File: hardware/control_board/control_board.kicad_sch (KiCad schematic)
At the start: 31 parts, among them J1 SWD, J2 Panel, J3 I2C, J4 SPI, SW1 Reset, U1 STM32F103C8T6, Y1 8MHz

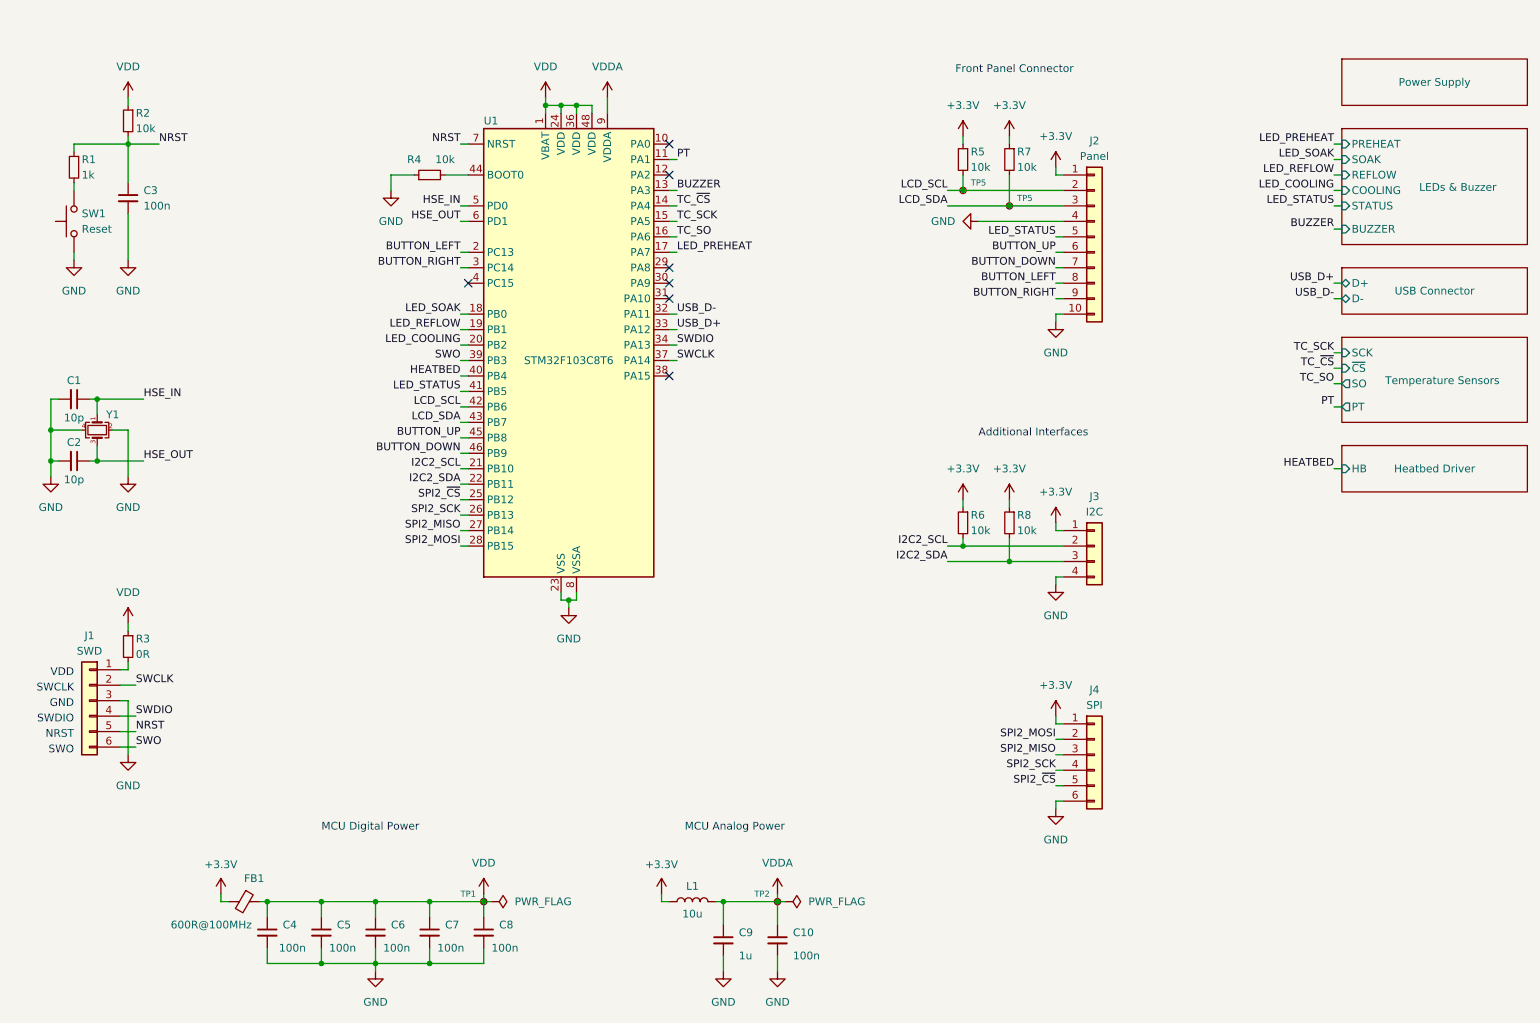
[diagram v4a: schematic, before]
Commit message: Place components on the control board PCB
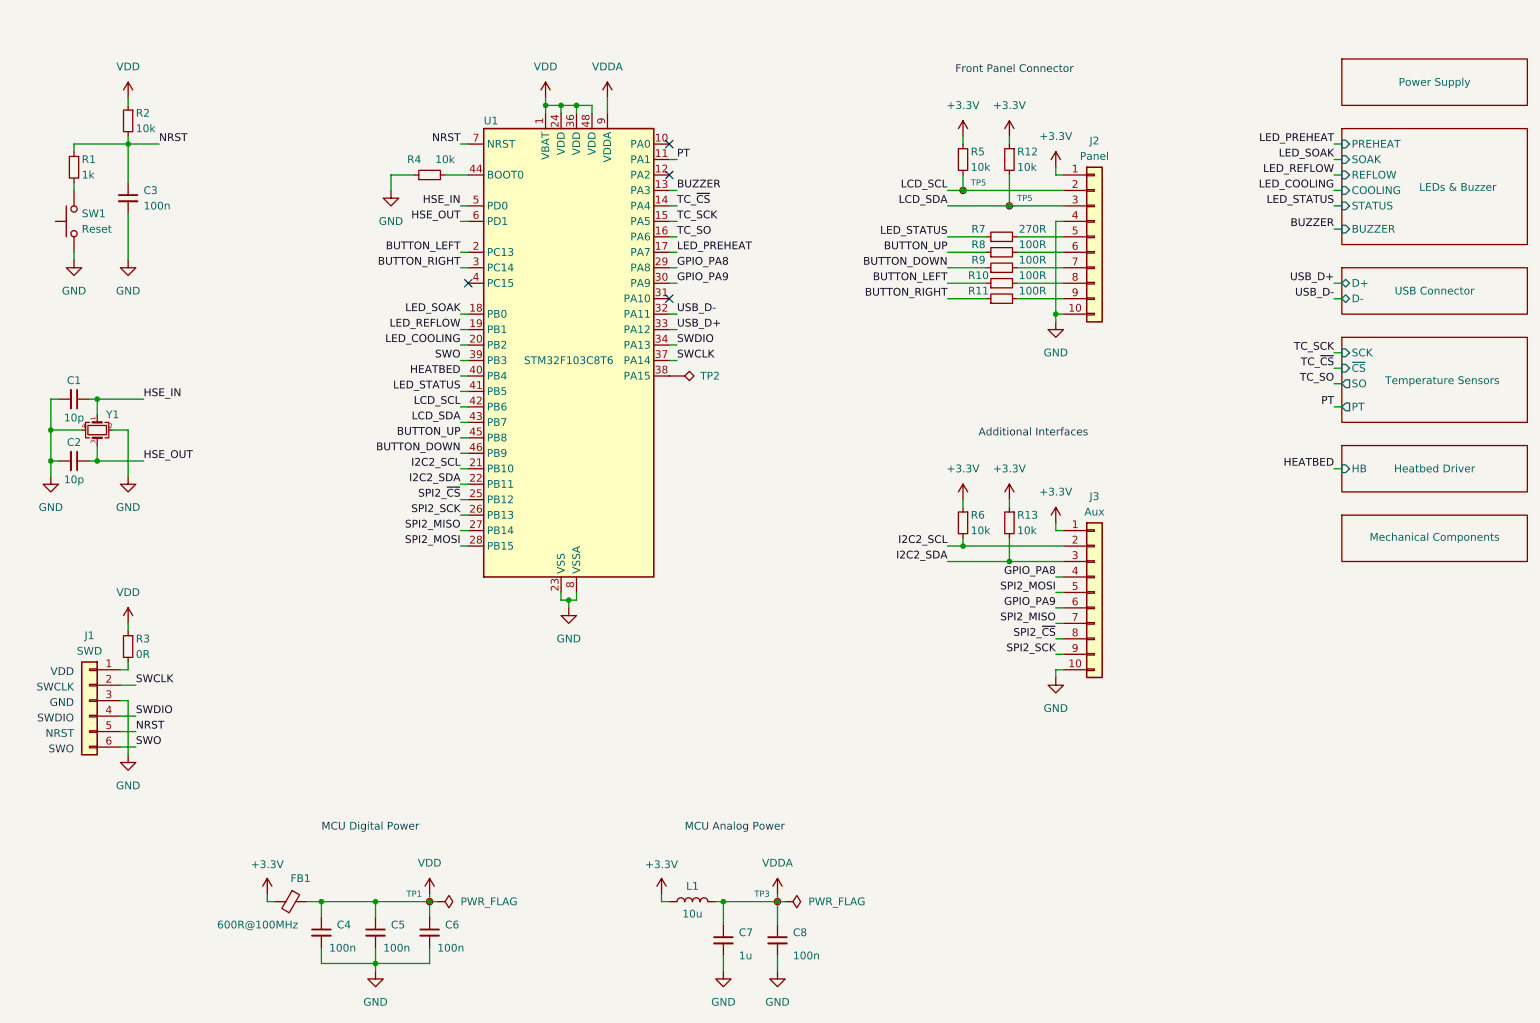
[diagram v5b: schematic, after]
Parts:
- removed C4, C5: 100n, Capacitor_SMD:C_0603_1608Metric, symbol Device:C_Small
- removed J3: I2C, Connector_PinHeader_2.54mm:PinHeader_1x04_P2.54mm_Vertical, symbol Connector_Generic:Conn_01x04
- removed J4: SPI, Connector_PinHeader_2.54mm:PinHeader_1x06_P2.54mm_Vertical, symbol Connector_Generic:Conn_01x06
- added J3: Aux, Connector_PinHeader_2.54mm:PinHeader_2x05_P2.54mm_Vertical, symbol Connector_Generic:Conn_01x10
- added R10, R11, R8, R9: 100R, Resistor_SMD:R_0603_1608Metric, symbol Device:R_Small
- added R7: 270R, Resistor_SMD:R_0603_1608Metric, symbol Device:R_Small
- added TP2: TestPoint_Alt, TestPoint:TestPoint_Pad_D1.0mm, symbol Connector:TestPoint_Alt
- renumbered C6 to C4, C7 to C5, C8 to C6, C9 to C7, C10 to C8, R7 to R12, R8 to R13, TP2 to TP3
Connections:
- net +3.3V: now also J3.1 (Pin_1)
- net BUTTON_DOWN: now also R9.1; no longer J2.7 (Pin_7)
- net BUTTON_LEFT: now also R10.1; no longer J2.8 (Pin_8)
- net BUTTON_RIGHT: now also R11.1; no longer J2.9 (Pin_9)
- net BUTTON_UP: now also R8.1; no longer J2.6 (Pin_6)
- net GND: now also J3.10 (Pin_10)
- net I2C2_SCL: now also J3.2 (Pin_2)
- net I2C2_SDA: now also J3.3 (Pin_3)
- net LED_STATUS: now also R7.1; no longer J2.5 (Pin_5)
- net SPI2_MISO: now also J3.7 (Pin_7)
- net SPI2_MOSI: now also J3.5 (Pin_5)
- net SPI2_SCK: now also J3.9 (Pin_9)
- net SPI2_~{CS}: now also J3.8 (Pin_8)
- net GPIO_PA8: now reaches U1.29 (PA8)
- net GPIO_PA8: now also J3.4 (Pin_4)
- net GPIO_PA9: now reaches U1.30 (PA9)
- net GPIO_PA9: now also J3.6 (Pin_6)
- net at U1.38 (PA15): now also TP2.1
- new net: J2.9 (Pin_9), R11.2
- new net: J2.6 (Pin_6), R8.2
- new net: J2.5 (Pin_5), R7.2
- new net: J2.7 (Pin_7), R9.2
- new net: J2.8 (Pin_8), R10.2
- no-connect marks 7 -> 4
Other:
- added sheet Mechanical Components (mechanical.kicad_sch)
- moved on the sheet: C4, C5, C6, FB1, TP1

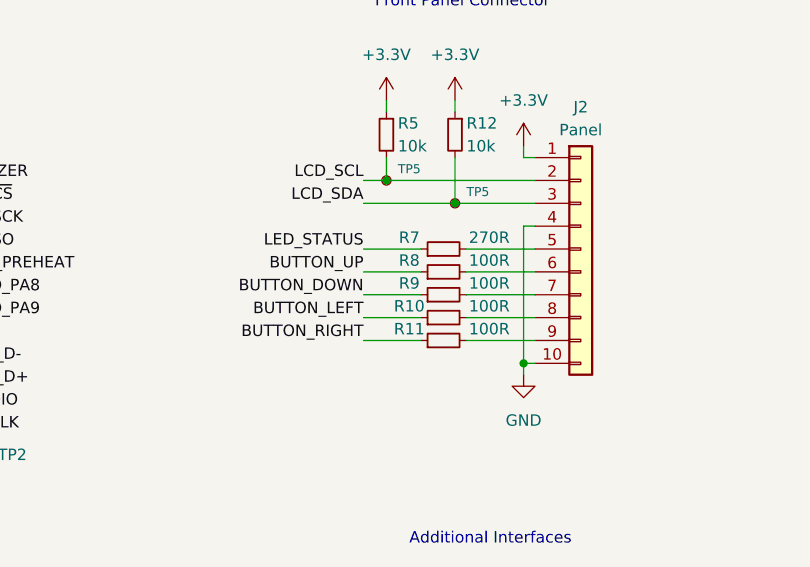
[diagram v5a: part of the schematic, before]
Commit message: Route front panel PCB tracks
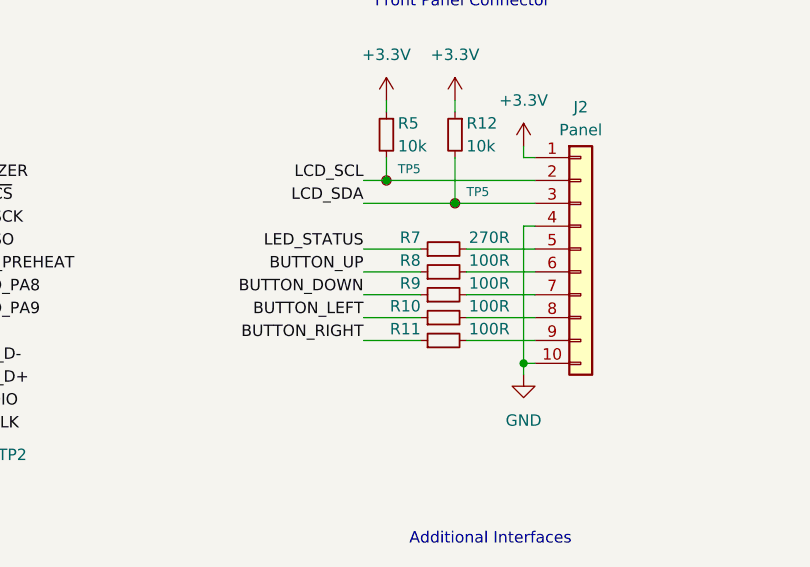
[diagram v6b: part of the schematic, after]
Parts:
- TP1, TP2, TP3, TP5: now left out of the parts list
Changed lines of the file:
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@@
   (symbol (lib_id "Device:R_Small") (at 185.42 68.58 90) (unit 1)
     (in_bom yes) (on_board yes) (dnp no)
-    (property "Reference" "R11" (at 181.61 67.31 90)
-      (effects (font (size 1.27 1.27)))
+    (property "Reference" "R11" (at 182.88 67.31 90)
+      (effects (font (size 1.27 1.27)) (justify left))
     )
     (property "Value" "100R" (at 190.5 67.31 90)
@@
   (symbol (lib_id "Device:R_Small") (at 185.42 60.96 90) (unit 1)
     (in_bom yes) (on_board yes) (dnp no)
-    (property "Reference" "R8" (at 181.61 59.69 90)
-      (effects (font (size 1.27 1.27)))
+    (property "Reference" "R8" (at 182.88 59.69 90)
+      (effects (font (size 1.27 1.27)) (justify left))
     )
     (property "Value" "100R" (at 190.5 59.69 90)
@@
   )
   (symbol (lib_id "Connector:TestPoint_Small") (at 148.59 167.64 0) (unit 1)
-    (in_bom yes) (on_board yes) (dnp no)
+    (in_bom no) (on_board yes) (dnp no)
     (property "Reference" "TP3" (at 144.78 166.37 0)
       (effects (font (size 1 1)) (justify left))
@@
   (symbol (lib_id "Device:R_Small") (at 185.42 58.42 90) (unit 1)
     (in_bom yes) (on_board yes) (dnp no)
-    (property "Reference" "R7" (at 181.61 57.15 90)
-      (effects (font (size 1.27 1.27)))
+    (property "Reference" "R7" (at 182.88 57.15 90)
+      (effects (font (size 1.27 1.27)) (justify left))
     )
     (property "Value" "270R" (at 190.5 57.15 90)
@@
   )
   (symbol (lib_id "Connector:TestPoint_Alt") (at 130.81 81.28 270) (unit 1)
-    (in_bom yes) (on_board yes) (dnp no)
+    (in_bom no) (on_board yes) (dnp no)
     (property "Reference" "TP2" (at 135.89 81.28 90)
       (effects (font (size 1.27 1.27)) (justify left))
@@
   )
   (symbol (lib_id "Connector:TestPoint_Small") (at 179.07 50.8 0) (unit 1)
-    (in_bom yes) (on_board yes) (dnp no)
+    (in_bom no) (on_board yes) (dnp no)
     (property "Reference" "TP5" (at 180.34 49.53 0)
       (effects (font (size 1 1)) (justify left))
@@
   (symbol (lib_id "Device:R_Small") (at 185.42 66.04 90) (unit 1)
     (in_bom yes) (on_board yes) (dnp no)
-    (property "Reference" "R10" (at 181.61 64.77 90)
-      (effects (font (size 1.27 1.27)))
+    (property "Reference" "R10" (at 182.88 64.77 90)
+      (effects (font (size 1.27 1.27)) (justify left))
     )
     (property "Value" "100R" (at 190.5 64.77 90)
@@
   )
   (symbol (lib_id "Connector:TestPoint_Small") (at 91.44 167.64 0) (unit 1)
-    (in_bom yes) (on_board yes) (dnp no)
+    (in_bom no) (on_board yes) (dnp no)
     (property "Reference" "TP1" (at 87.63 166.37 0)
       (effects (font (size 1 1)) (justify left))
@@
   (symbol (lib_id "Device:R_Small") (at 185.42 63.5 90) (unit 1)
     (in_bom yes) (on_board yes) (dnp no)
-    (property "Reference" "R9" (at 181.61 62.23 90)
-      (effects (font (size 1.27 1.27)))
+    (property "Reference" "R9" (at 182.88 62.23 90)
+      (effects (font (size 1.27 1.27)) (justify left))
     )
     (property "Value" "100R" (at 190.5 62.23 90)
@@
   )
   (symbol (lib_id "Connector:TestPoint_Small") (at 186.69 53.34 0) (unit 1)
-    (in_bom yes) (on_board yes) (dnp no)
+    (in_bom no) (on_board yes) (dnp no)
     (property "Reference" "TP5" (at 187.96 52.07 0)
       (effects (font (size 1 1)) (justify left))

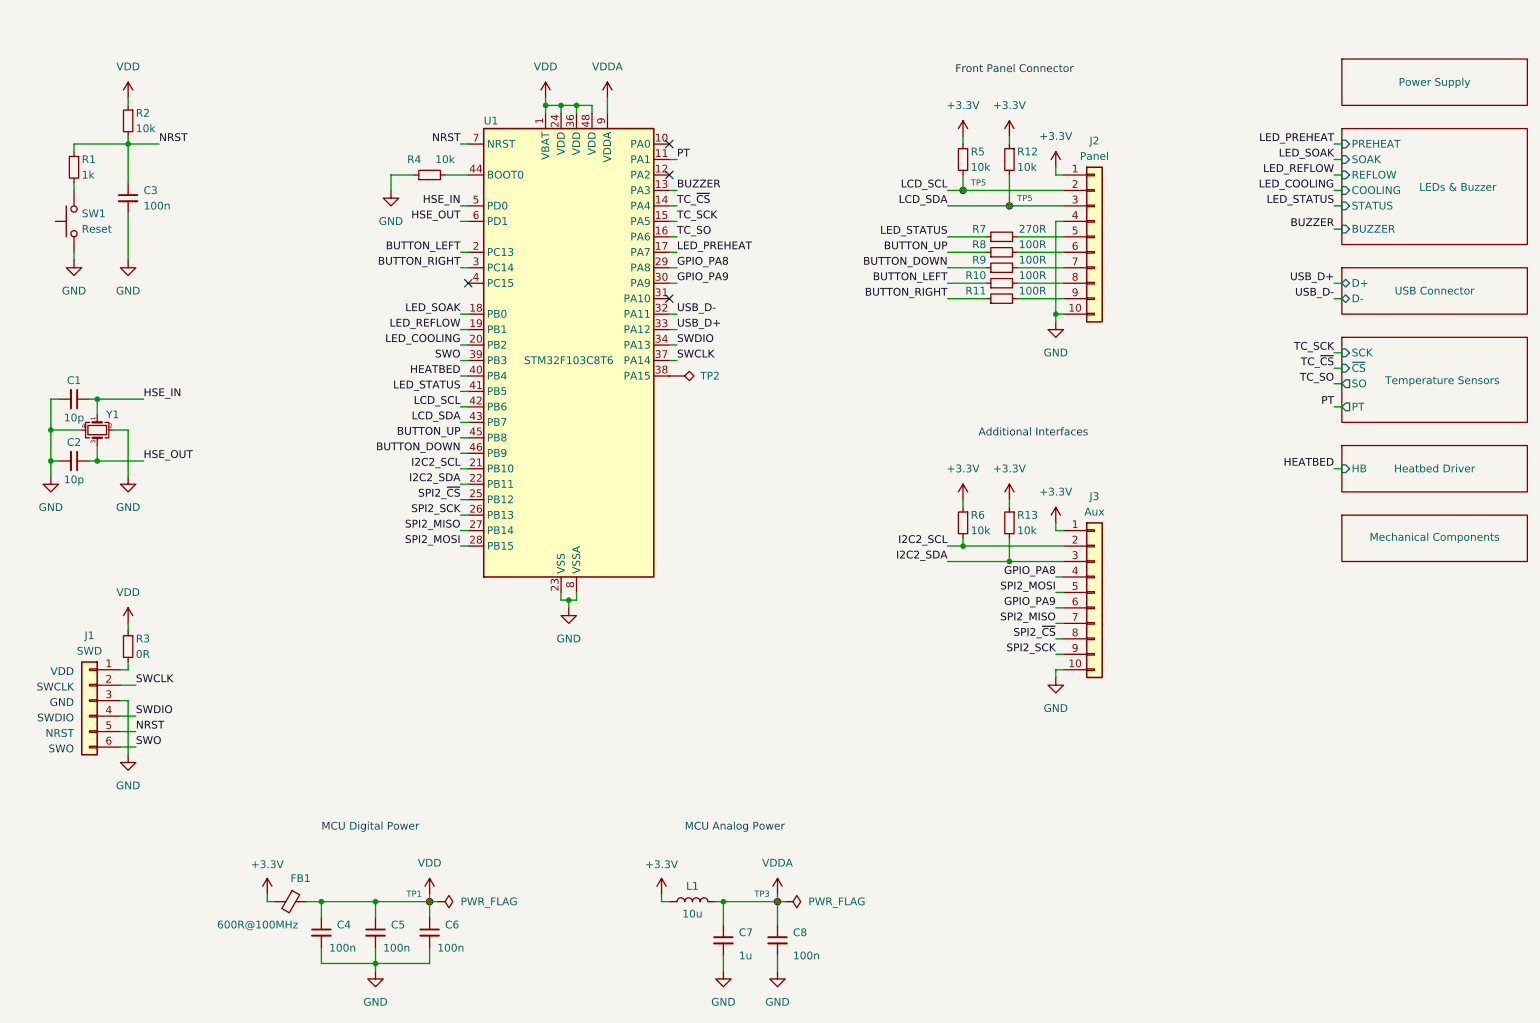
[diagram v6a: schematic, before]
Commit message: Route control board PCB tracks
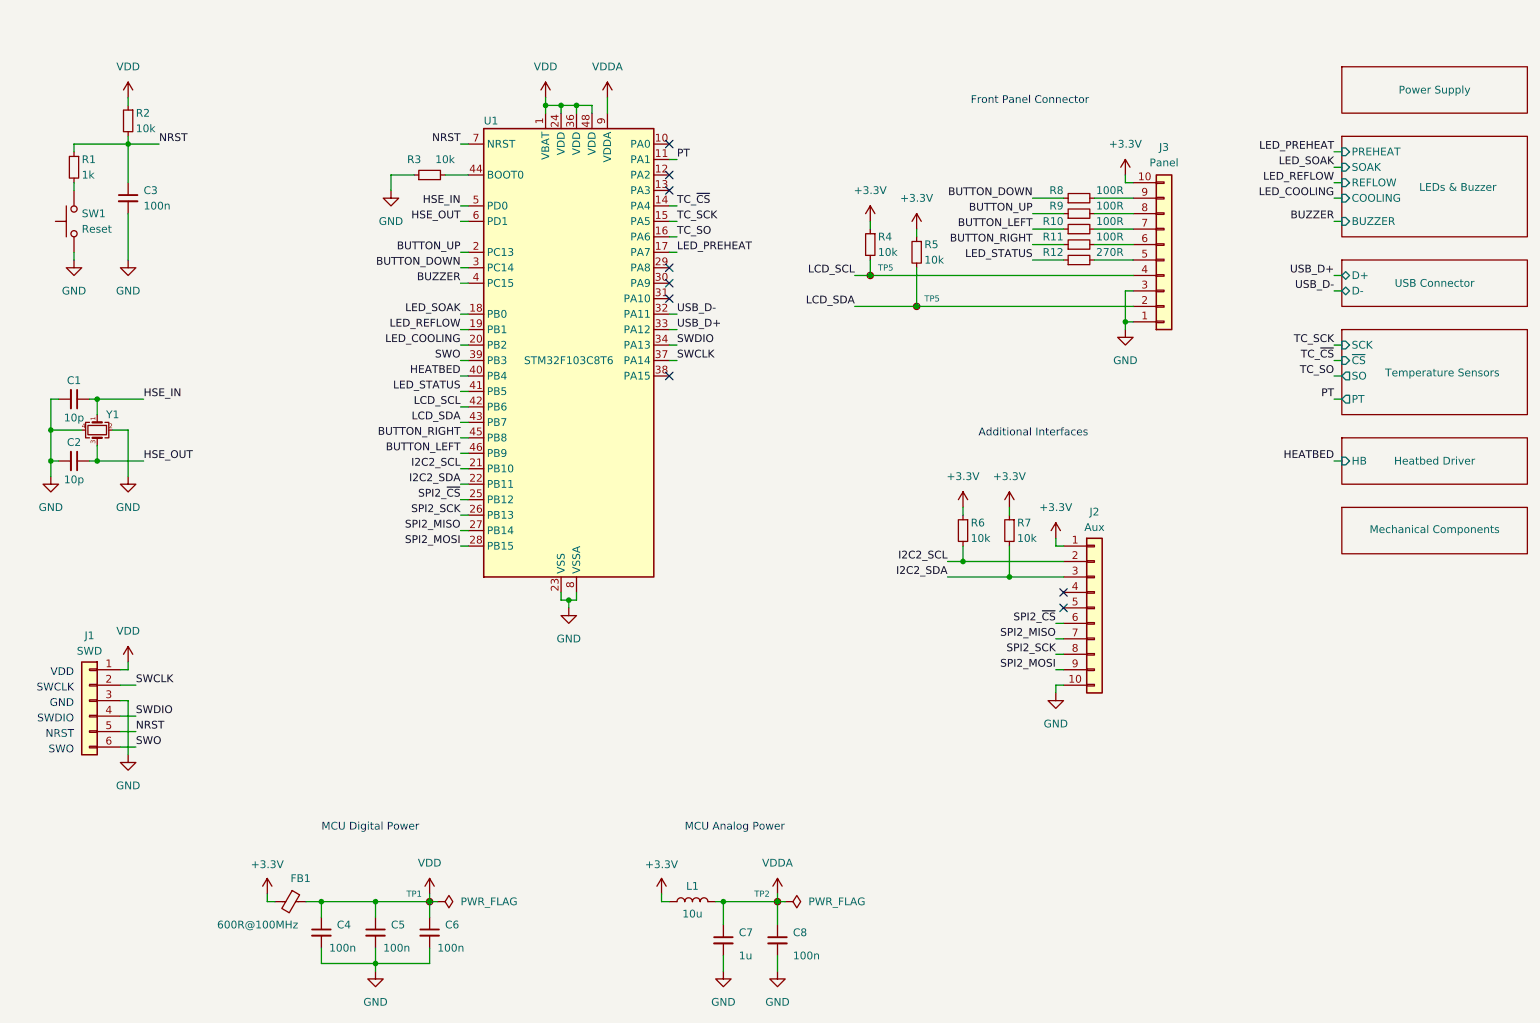
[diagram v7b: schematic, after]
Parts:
- removed R3: 0R, Resistor_SMD:R_0603_1608Metric, symbol Device:R_Small
- removed TP2: TestPoint_Alt, TestPoint:TestPoint_Pad_D1.0mm, symbol Connector:TestPoint_Alt
- renumbered J3 to J2, J2 to J3, R7 to R12, R4 to R3, R5 to R4, R12 to R5, R13 to R7, R9 to R8, R8 to R9, TP3 to TP2
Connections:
- net +3.3V: now also J3.10 (Pin_10); no longer J3.1 (Pin_1)
- net BUTTON_DOWN: now also U1.3 (PC14); no longer U1.46 (PB9)
- net BUTTON_LEFT: now also U1.46 (PB9); no longer U1.2 (PC13)
- net BUTTON_RIGHT: now also U1.45 (PB8); no longer U1.3 (PC14)
- net BUTTON_UP: now also U1.2 (PC13); no longer U1.45 (PB8)
- net BUZZER: now also U1.4 (PC15); no longer U1.13 (PA3)
- net GND: now also J3.1 (Pin_1), J3.3 (Pin_3); no longer J3.10 (Pin_10), J3.4 (Pin_4)
- net LCD_SCL: now also J3.4 (Pin_4); no longer J3.2 (Pin_2)
- net LCD_SDA: now also J3.2 (Pin_2); no longer J3.3 (Pin_3)
- net SPI2_MOSI: now also J2.9 (Pin_9); no longer J2.5 (Pin_5)
- net SPI2_SCK: now also J2.8 (Pin_8); no longer J2.9 (Pin_9)
- net SPI2_~{CS}: now also J2.6 (Pin_6); no longer J2.8 (Pin_8)
- net VDD: now also J1.1 (Pin_1)
- net at R11.2: now also J3.6 (Pin_6); no longer J3.9 (Pin_9)
- net at R9.2: now also J3.8 (Pin_8); no longer J3.6 (Pin_6)
- net at J3.7 (Pin_7): now also R10.2; no longer R8.2
- net GPIO_PA8: no longer names the net of U1.29 (PA8)
- net GPIO_PA8: no longer J2.4 (Pin_4)
- net GPIO_PA9: no longer names the net of U1.30 (PA9)
- net GPIO_PA9: no longer J2.6 (Pin_6)
- new net: J3.9 (Pin_9), R8.2
- no-connect marks 4 -> 9
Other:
- sheet LEDs & Buzzer ports: added none; removed STATUS
- moved on the sheet: J2, J3, R10, R11, R12, R4, R5, R6, R7, R8, R9, TP5
